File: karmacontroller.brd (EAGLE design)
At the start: 100 x 50 mm, 19 parts

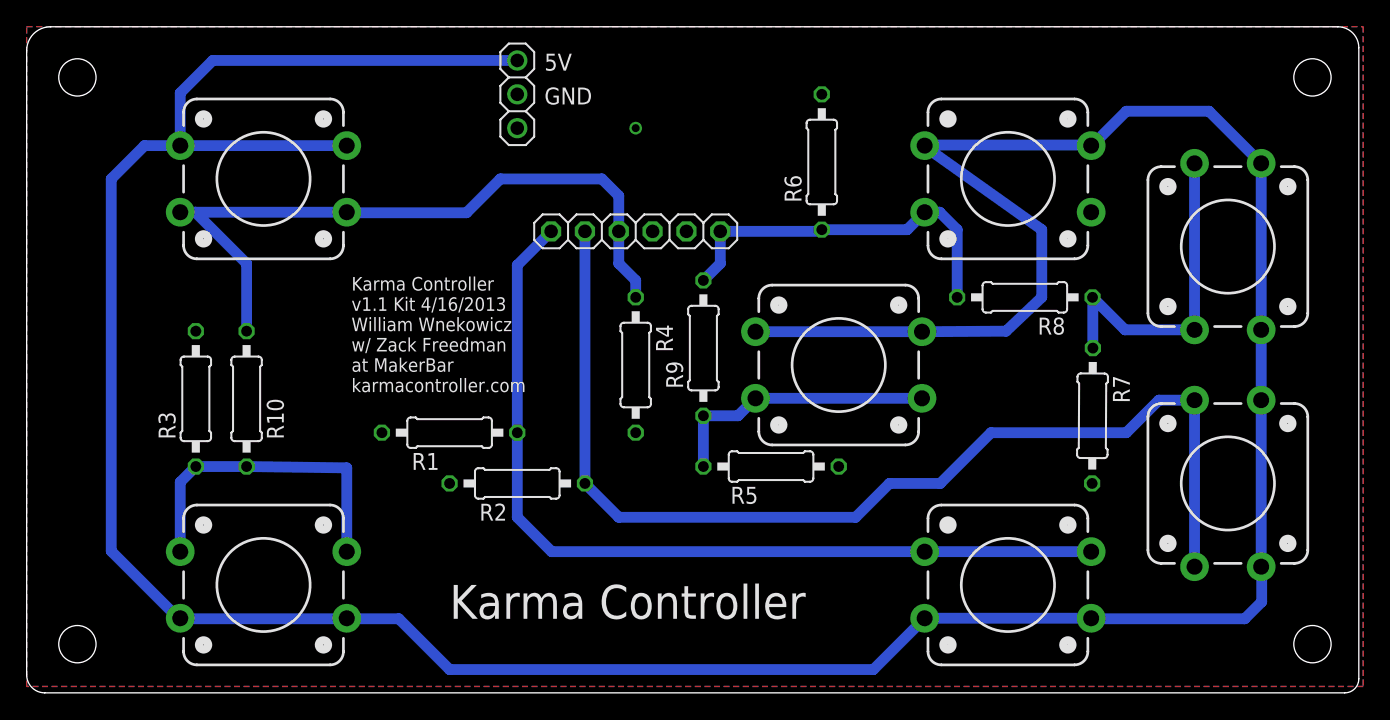
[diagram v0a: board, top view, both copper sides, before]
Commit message: Upgraded board and software
- I changed all the resistors to the Sparkfun AXIAL-0.3 and rerouted
everything.
- I changed the mask limit to 25mil.
- I moved the "Karma Controller" text over to the left.
- I hid the tOrigins layer. These are the crosshairs.
- I updated the date to 6/25/2013
- I updated the software to use the analog values for the new 4.7K
resistor
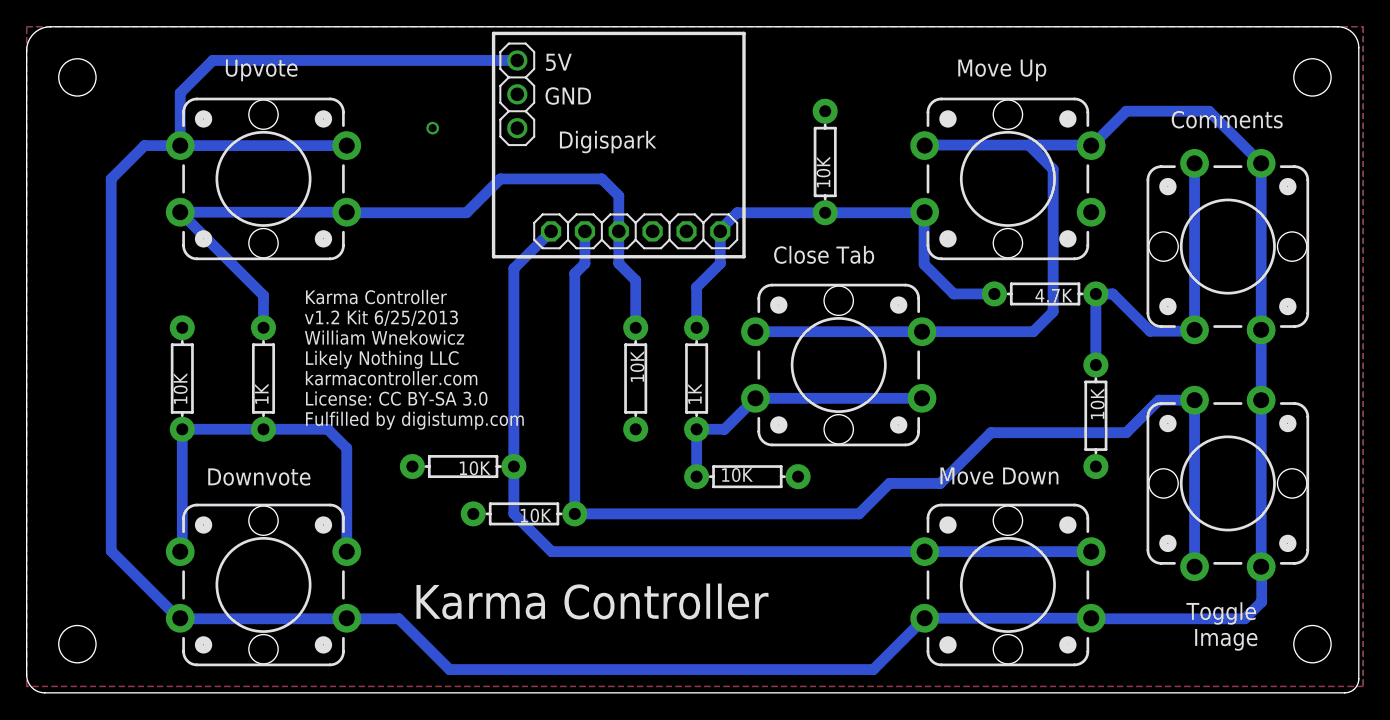
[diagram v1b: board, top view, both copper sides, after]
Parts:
- R1, R2, R3, R4, R5, R6, R7: value 10k -> 10K; device rcl:0207/10 -> SparkFun-Resistors:AXIAL-0.3
- R10, R9: value 1k -> 1K; device rcl:0207/10 -> SparkFun-Resistors:AXIAL-0.3
- R8: value 3.3k -> 4.7K; device rcl:0207/10 -> SparkFun-Resistors:AXIAL-0.3
- moved R1 2.74 mm to (32.8, 47.0)
- moved R2 2.34 mm to (37.3, 43.4)
- moved R9 2.34 mm to (50.3, 53.6)
- moved R10 1.98 mm to (17.8, 53.6)
- moved R5 1.93 mm to (54.1, 46.2)
- moved R3 1.83 mm to (11.7, 53.6)
- moved R8 1.55 mm to (76.5, 59.9)
- moved R4 1.02 mm to (45.7, 53.6)
- moved R6 0.25 mm to (59.9, 69.8)
- moved R7 0.25 mm to (80.3, 50.8), turned to 270 degrees
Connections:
- net DOWN: now also R7.P$1, R8.P$1; no longer R7.1, R8.1
- net GND: now also R1.P$2, R2.P$2, R3.P$2, R4.P$2, R5.P$2, R6.P$2, R7.P$2; no longer R1.2, R2.2, R3.2, R4.2, R5.2, R6.2, R7.2
- net N$1: now also R2.P$1; no longer R2.1
- net N$2: now also R1.P$1; no longer R1.1
- net N$4: now also R10.P$2, R4.P$1; no longer R10.2, R4.1
- net N$5: now also R5.P$1, R9.P$1; no longer R5.1, R9.1
- net N$6: now also R6.P$1, R8.P$2, R9.P$2; no longer R6.1, R8.2, R9.2
- net N$7: now also R10.P$1, R3.P$1; no longer R10.1, R3.1
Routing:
- net N$6: track 28.2 -> 34.1 mm
- net N$7: track 24.5 -> 29.9 mm
- net N$4: track 53.2 -> 56.2 mm
- net N$1: track 81.9 -> 84.1 mm
- net 5V: track 269.1 -> 266.9 mm
- net DOWN: track 25.0 -> 26.4 mm
- net N$5: track 20.8 -> 21.4 mm
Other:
- board text added: "Close Tab"
- board text added: "Comments"
- board text added: "Digispark"
- board text added: "Downvote"
- board text added: "Image"
- board text added: "Karma Controller v1.2 Kit 6/25/2013 William Wnekowicz Likely Nothing LLC karmacontroller.com License: CC BY-SA 3.0 Fulfilled by digistump.com"
- board text added: "Move Down"
- board text added: "Move Up"
- board text added: "Toggle"
- board text added: "Upvote"
- board text removed: "Karma Controller v1.1 Kit 4/16/2013 William Wnekowicz w/ Zack Freedman at MakerBar karmacontroller.com"
